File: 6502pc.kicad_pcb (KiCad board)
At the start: 2 copper layers, 100.5 x 115 mm, 42 parts, among them J1 DB9 Serial Port, J2 USB_B, J3 Conn_01x08_Pin, J4 Conn_01x08_Pin, J5 Conn_01x16_Socket, J6 SD-Card Board, J7 FTDI Socket, J9 Expansion / Diag Port, SW1 Reset Switch, SW2 SW_SPST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

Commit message: update
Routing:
- net A9: track 23.3 -> 92.0 mm
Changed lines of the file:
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@@
 		(legacy_teardrops no)
 	)
-	(paper "A4")
+	(paper "A3")
 	(layers
 		(0 "F.Cu" signal)
@@
 		(net 55)
 	)
+	(segment
+		(start 76.39895 119.156)
+		(end 115.53695 119.156)
+		(width 0.2)
+		(layer "B.Cu")
+		(net 55)
+	)
+	(segment
+		(start 120.77395 113.919)
+		(end 127.508 113.919)
+		(width 0.2)
+		(layer "B.Cu")
+		(net 55)
+	)
+	(segment
+		(start 61.5 117.94)
+		(end 75.18295 117.94)
+		(width 0.2)
+		(layer "B.Cu")
+		(net 55)
+	)
+	(segment
+		(start 75.18295 117.94)
+		(end 76.39895 119.156)
+		(width 0.2)
+		(layer "B.Cu")
+		(net 55)
+	)
+	(segment
+		(start 115.53695 119.156)
+		(end 120.77395 113.919)
+		(width 0.2)
+		(layer "B.Cu")
+		(net 55)
+	)

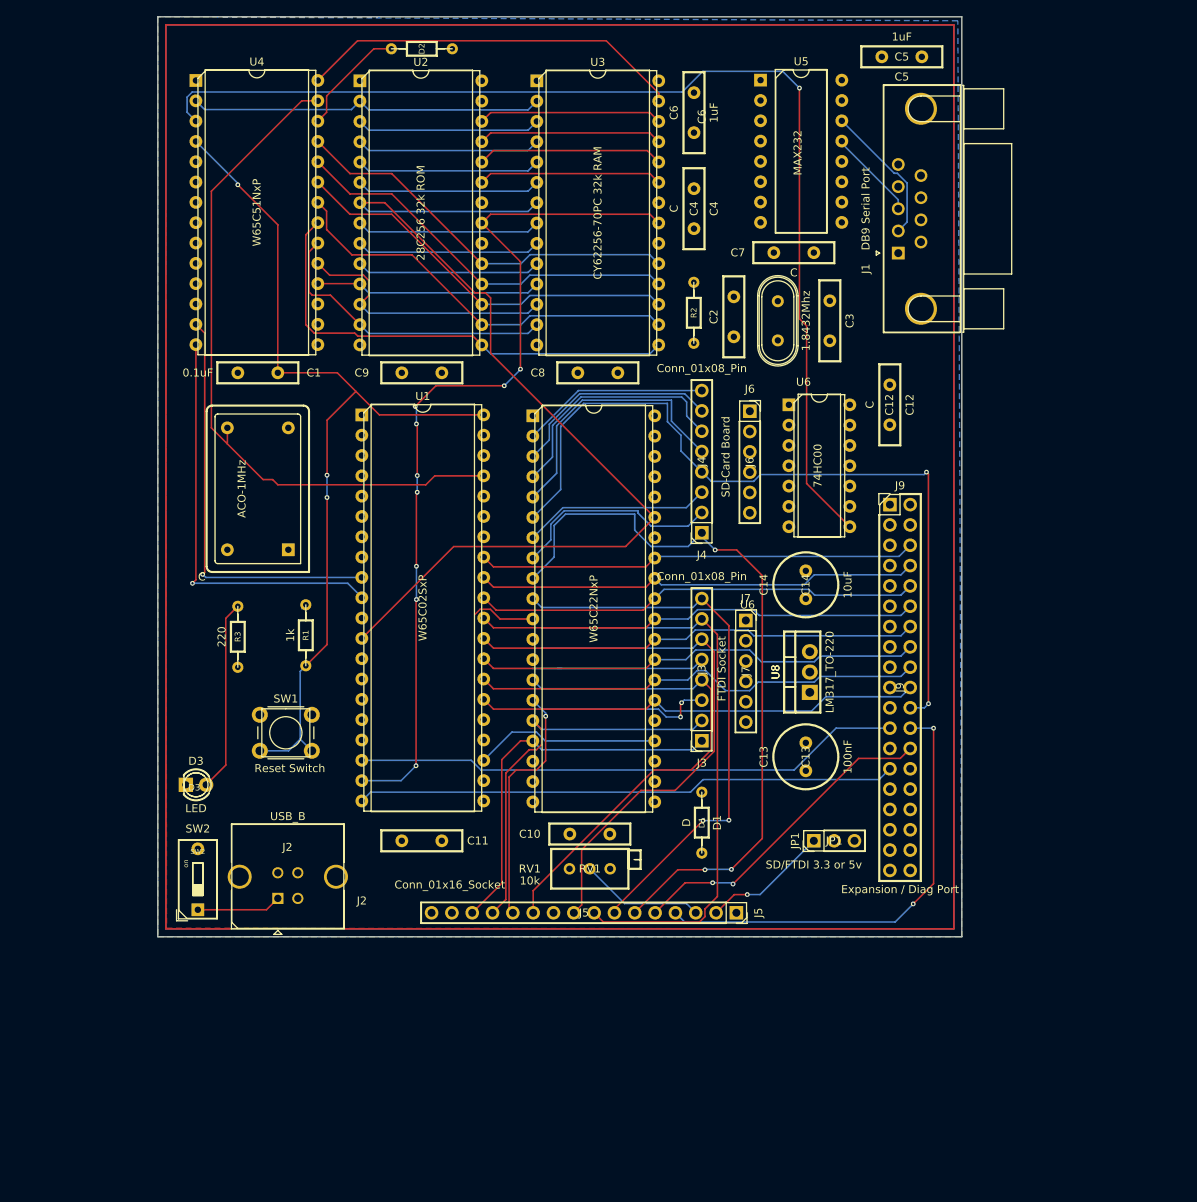
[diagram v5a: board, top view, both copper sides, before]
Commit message: Routing and added auto reset
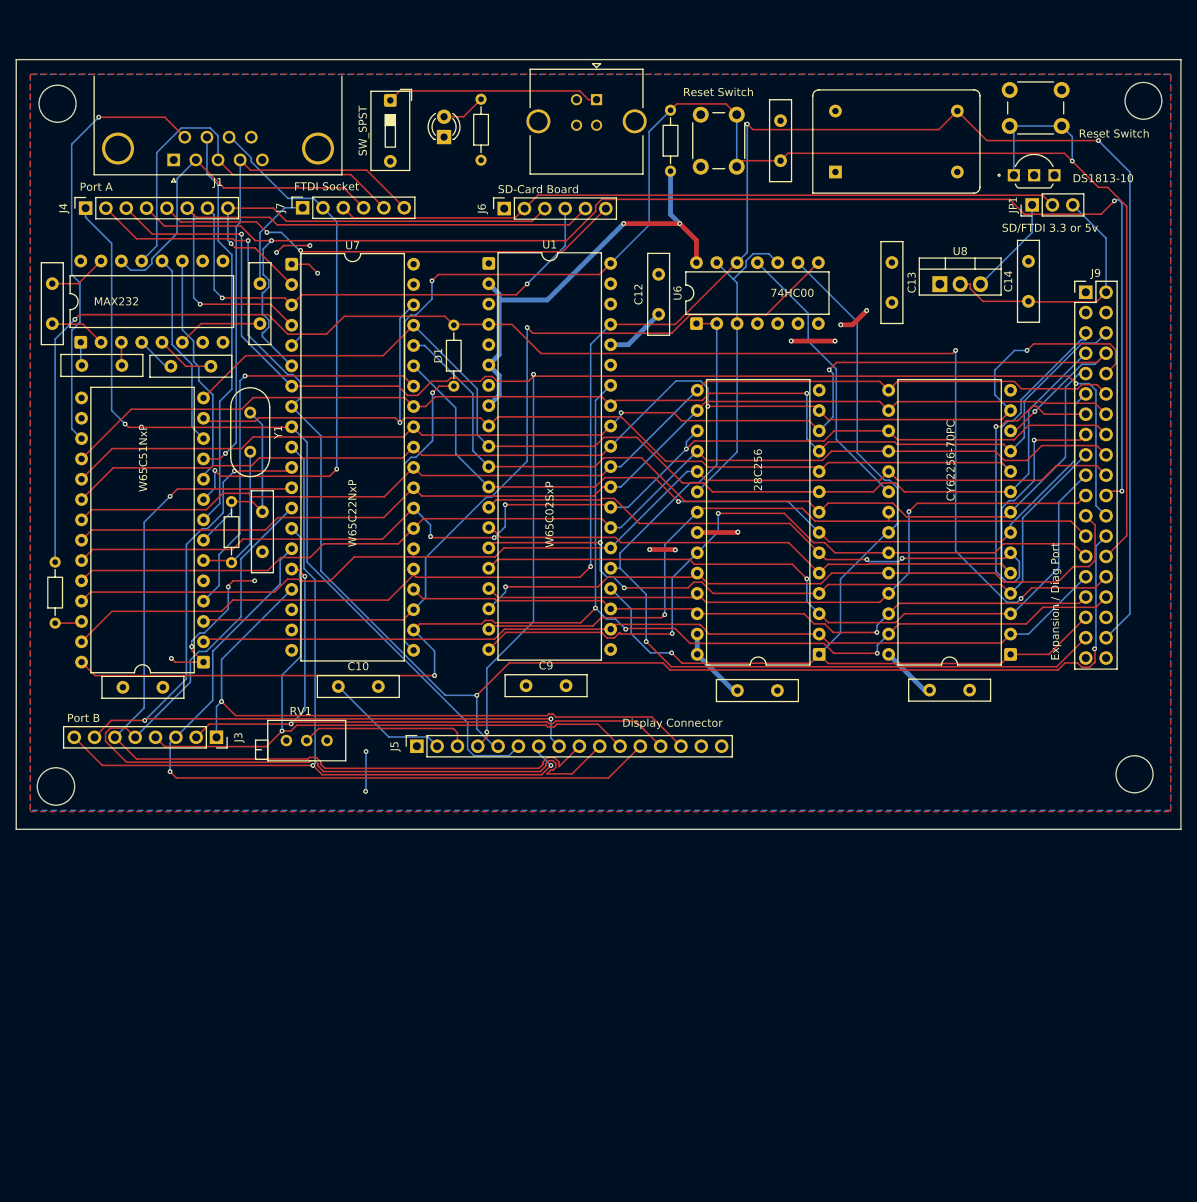
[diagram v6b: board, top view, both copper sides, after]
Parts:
- added SW3: Reset Switch, Button_Switch_THT:SW_PUSH_6mm, F.Cu at (142.5, 34.1)
- added U9: DS1813-10, x:21-0248A_MXM, F.Cu at (143.0, 44.8)
- C13, C14: footprint Capacitor_THT:C_Radial_D8.0mm_H11.5mm_P3.50mm -> Capacitor_THT:C_Disc_D10.0mm_W2.5mm_P5.00mm
- J1: footprint Connector_Dsub:DSUB-9_Male_Horizontal_P2.77x2.84mm_EdgePinOffset4.94mm_Housed_MountingHolesOffset4.94mm -> x:DSUB-9_Female_Horizontal_P2.77x2.84mm_EdgePinOffset7.70mm_Housed_MountingHolesOffset9.12mm
- J3: value Conn_01x08_Pin -> Port B
- J4: value Conn_01x08_Pin -> Port A
- J5: value Conn_01x16_Socket -> Display Connector
- moved C5 111.9 mm to (26.5, 68.6), turned to 0 degrees
- moved J2 107.5 mm to (90.8, 35.4), turned to 0 degrees
- moved SW2 104.0 mm to (65.1, 35.5), turned to -90 degrees
- moved U3 93.0 mm to (142.6, 104.7), turned to 180 degrees
- moved U2 91.9 mm to (118.7, 104.7), turned to 180 degrees
- moved J1 91.3 mm to (38.0, 42.9), turned to 180 degrees
- moved U5 91.1 mm to (26.4, 65.7), turned to 90 degrees
- moved SW1 87.9 mm to (103.9, 43.7), turned to 90 degrees
- moved D3 87.2 mm to (71.8, 40.0), turned to 90 degrees
- moved J4 87.1 mm to (27.0, 48.9), turned to 90 degrees
- moved JP1 84.0 mm to (145.3, 48.5)
- moved D2 83.2 mm to (23.2, 100.8), turned to 90 degrees
- moved X1 83.1 mm to (120.7, 44.4), turned to 0 degrees
- moved C4 82.0 mm to (22.8, 63.4), turned to 90 degrees
- moved J7 75.7 mm to (54.1, 48.9), turned to 90 degrees
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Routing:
- net IRQ: track 0.00 -> 193.7 mm, vias 0 -> 3
- net clock: track 87.0 -> 248.3 mm, vias 0 -> 3
- net PA6: track 66.9 -> 196.0 mm, vias 2 -> 3
- net Reset: track 115.1 -> 243.3 mm
- net A14: track 0.29 -> 127.0 mm, vias 0 -> 1
- net PA5: track 80.6 -> 206.7 mm, vias 2 -> 4
- net RW: track 48.4 -> 174.1 mm, vias 0 -> 4
- net A15: track 0.00 -> 108.2 mm, vias 0 -> 1
- net VCC: track 17.7 -> 113.7 mm, vias 1 -> 4
- net Net-(J6-Pin_2): track 0.00 -> 90.9 mm
- net PB3: track 22.2 -> 111.7 mm
- net A2: track 23.0 -> 111.5 mm
- net PA4: track 98.3 -> 185.3 mm, vias 2 -> 3
- net A4: track 23.0 -> 107.4 mm, vias 0 -> 3
- net A5: track 23.0 -> 94.4 mm, vias 0 -> 1
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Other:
- board size 100.5 x 115 mm -> 145.6 x 96.2 mm

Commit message: bom and sound app
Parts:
- J9: footprint Connector_PinHeader_2.54mm:PinHeader_2x19_P2.54mm_Vertical -> Connector_PinSocket_2.54mm:PinSocket_2x19_P2.54mm_Vertical
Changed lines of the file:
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@@
 			(unlocked yes)
 			(layer "F.SilkS")
-			(hide yes)
 			(effects
 				(font
@@
 		)
 		(property "Value" "DS1813-10"
-			(at 11.176 0.4064 0)
+			(at 2.54 0 0)
 			(unlocked yes)
-			(layer "F.SilkS")
+			(layer "F.Fab")
 			(effects
 				(font
@@
 		)
 	)
-	(footprint "Connector_PinHeader_2.54mm:PinHeader_2x19_P2.54mm_Vertical"
+	(footprint "Connector_PinSocket_2.54mm:PinSocket_2x19_P2.54mm_Vertical"
 		(layer "F.Cu")
 		(at 151.9936 59.436)
-		(descr "Through hole straight pin header, 2x19, 2.54mm pitch, double rows")
-		(tags "Through hole pin header THT 2x19 2.54mm double row")
+		(descr "Through hole straight socket strip, 2x19, 2.54mm pitch, double cols (from Kicad 4.0.7), script generated")
+		(tags "Through hole socket strip THT 2x19 2.54mm double row")
 		(property "Reference" "J9"
-			(at 1.27 -2.38 0)
+			(at -1.27 -2.77 0)
 			(layer "F.SilkS")
 			(effects
@@
 		)
 		(property "Value" "Expansion / Diag Port"
-			(at -3.81 38.6588 90)
-			(layer "F.SilkS")
+			(at -1.27 48.49 0)
+			(layer "F.Fab")
 			(effects
 				(font
@@
 		(attr through_hole)
 		(fp_line
-			(start -1.38 -1.38)
-			(end 0 -1.38)
+			(start -3.87 -1.33)
+			(end -3.87 47.05)
 			(stroke
 				(width 0.12)
@@
 		)
 		(fp_line
-			(start -1.38 0)
-			(end -1.38 -1.38)
+			(start -3.87 -1.33)
+			(end -1.27 -1.33)
 			(stroke
 				(width 0.12)
@@
 		)
 		(fp_line
-			(start -1.38 1.27)
-			(end -1.38 47.1)
+			(start -3.87 47.05)
+			(end 1.33 47.05)
 			(stroke
 				(width 0.12)
@@
 		)
 		(fp_line
-			(start -1.38 1.27)
-			(end 1.27 1.27)
+			(start -1.27 -1.33)
+			(end -1.27 1.27)
 			(stroke
 				(width 0.12)
@@
 		)
 		(fp_line
-			(start -1.38 47.1)
-			(end 3.92 47.1)
+			(start -1.27 1.27)
+			(end 1.33 1.27)
 			(stroke
 				(width 0.12)
@@
 		)
 		(fp_line
-			(start 1.27 -1.38)
-			(end 3.92 -1.38)
+			(start 0 -1.33)
+			(end 1.33 -1.33)
 			(stroke
 				(width 0.12)
@@
 		)
 		(fp_line
-			(start 1.27 1.27)
-			(end 1.27 -1.38)
+			(start 1.33 -1.33)
+			(end 1.33 0)
 			(stroke
 				(width 0.12)
@@
 		)
 		(fp_line
-			(start 3.92 -1.38)
-			(end 3.92 47.1)
+			(start 1.33 1.27)
+			(end 1.33 47.05)
 			(stroke
 				(width 0.12)
@@
 		)
 		(fp_line
-			(start -1.77 -1.78)
-			(end -1.77 47.49)
+			(start -4.34 -1.8)
+			(end 1.76 -1.8)
 			(stroke
 				(width 0.05)
@@
 		)
 		(fp_line
-			(start -1.77 47.49)
-			(end 4.32 47.49)
+			(start -4.34 47.5)
+			(end -4.34 -1.8)
 			(stroke
 				(width 0.05)
@@
 		)
 		(fp_line
-			(start 4.32 -1.78)
-			(end -1.77 -1.78)
+			(start 1.76 -1.8)
+			(end 1.76 47.5)
 			(stroke
 				(width 0.05)
@@
 		)
 		(fp_line
-			(start 4.32 47.49)
-			(end 4.32 -1.78)
+			(start 1.76 47.5)
+			(end -4.34 47.5)
 			(stroke
 				(width 0.05)
@@
 		)
 		(fp_line
-			(start -1.27 0)
-			(end 0 -1.27)
+			(start -3.81 -1.27)
+			(end 0.27 -1.27)
 			(stroke
 				(width 0.1)
@@
 		)
 		(fp_line
-			(start -1.27 46.99)
-			(end -1.27 0)
+			(start -3.81 46.99)
+			(end -3.81 -1.27)
 			(stroke
 				(width 0.1)
@@
 		)
 		(fp_line
-			(start 0 -1.27)
-			(end 3.81 -1.27)
+			(start 0.27 -1.27)
+			(end 1.27 -0.27)
 			(stroke
 				(width 0.1)
@@
 		)
 		(fp_line
-			(start 3.81 -1.27)
-			(end 3.81 46.99)
+			(start 1.27 -0.27)
+			(end 1.27 46.99)
 			(stroke
 				(width 0.1)
@@
 		)
 		(fp_line
-			(start 3.81 46.99)
-			(end -1.27 46.99)
+			(start 1.27 46.99)
+			(end -3.81 46.99)
 			(stroke
 				(width 0.1)
@@
 		)
 		(fp_text user "${REFERENCE}"
-			(at 1.27 22.86 90)
+			(at -1.27 22.86 90)
 			(layer "F.Fab")
 			(effects
@@
 		)
 		(pad "2" thru_hole circle
-			(at 2.54 0)
+			(at -2.54 0)
 			(size 1.7 1.7)
 			(drill 1)
@@
 		)
 		(pad "4" thru_hole circle
-			(at 2.54 2.54)
+			(at -2.54 2.54)
 			(size 1.7 1.7)
 			(drill 1)
@@
 		)
 		(pad "6" thru_hole circle
-			(at 2.54 5.08)
+			(at -2.54 5.08)
 			(size 1.7 1.7)
 			(drill 1)
@@
 		)
 		(pad "8" thru_hole circle
-			(at 2.54 7.62)
+			(at -2.54 7.62)
 			(size 1.7 1.7)
 			(drill 1)
@@
 		)
 		(pad "10" thru_hole circle
-			(at 2.54 10.16)
+			(at -2.54 10.16)
 			(size 1.7 1.7)
 			(drill 1)
@@
 		)
 		(pad "12" thru_hole circle
-			(at 2.54 12.7)
+			(at -2.54 12.7)
 			(size 1.7 1.7)
 			(drill 1)
@@
 		)
 		(pad "14" thru_hole circle
-			(at 2.54 15.24)
+			(at -2.54 15.24)
 			(size 1.7 1.7)
 			(drill 1)
@@
 		)
 		(pad "16" thru_hole circle
-			(at 2.54 17.78)
+			(at -2.54 17.78)
 			(size 1.7 1.7)
 			(drill 1)
@@
 		)
 		(pad "18" thru_hole circle
-			(at 2.54 20.32)
+			(at -2.54 20.32)
 			(size 1.7 1.7)
 			(drill 1)
@@
 		)
 		(pad "20" thru_hole circle
-			(at 2.54 22.86)
+			(at -2.54 22.86)
 			(size 1.7 1.7)
 			(drill 1)
@@
 		)
 		(pad "22" thru_hole circle
-			(at 2.54 25.4)
+			(at -2.54 25.4)
 			(size 1.7 1.7)
 			(drill 1)
@@
 		)
 		(pad "24" thru_hole circle
-			(at 2.54 27.94)
+			(at -2.54 27.94)
 			(size 1.7 1.7)
 			(drill 1)
@@
 		)
 		(pad "26" thru_hole circle
-			(at 2.54 30.48)
+			(at -2.54 30.48)
 			(size 1.7 1.7)
 			(drill 1)
@@
 		)
 		(pad "28" thru_hole circle
-			(at 2.54 33.02)
+			(at -2.54 33.02)
 			(size 1.7 1.7)
 			(drill 1)
@@
 		)
 		(pad "30" thru_hole circle
-			(at 2.54 35.56)
+			(at -2.54 35.56)
 			(size 1.7 1.7)
 			(drill 1)
@@
 		)
 		(pad "32" thru_hole circle
-			(at 2.54 38.1)
+			(at -2.54 38.1)
 			(size 1.7 1.7)
 			(drill 1)
@@
 		)
 		(pad "34" thru_hole circle
-			(at 2.54 40.64)
+			(at -2.54 40.64)
 			(size 1.7 1.7)
 			(drill 1)
@@
 		)
 		(pad "36" thru_hole circle
-			(at 2.54 43.18)
+			(at -2.54 43.18)
 			(size 1.7 1.7)
 			(drill 1)
@@
 		)
 		(pad "38" thru_hole circle
-			(at 2.54 45.72)
+			(at -2.54 45.72)
 			(size 1.7 1.7)
 			(drill 1)
@@
 		)
 		(embedded_fonts no)
-		(model "${KICAD9_3DMODEL_DIR}/Connector_PinHeader_2.54mm.3dshapes/PinHeader_2x19_P2.54mm_Vertical.step"
+		(model "${KICAD9_3DMODEL_DIR}/Connector_PinSocket_2.54mm.3dshapes/PinSocket_2x19_P2.54mm_Vertical.step"
 			(offset
 				(xyz 0 0 0)

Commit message: x5
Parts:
- added REF**: Logo, x:Logo, F.Cu at (131.1, 102.5)
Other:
- board text added: "BY TOM SMITH V1"
